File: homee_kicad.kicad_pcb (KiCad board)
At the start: 2 copper layers, 28 parts, among them J1 Screw_Terminal_01x02, J2 USB_B_Micro, J3 Screw_Terminal_01x02, K1 SANYOU_SRD_Form_C, Q2 Q_NPN_Darlington_CBE, T1 Transformer_1P_1S, U1 ESP-01v090, U2 LD1117S33TR_SOT223, U4 PC817

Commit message: j'ai tt fini je suis le goat (PS pas verif par le prof)
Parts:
- removed C4: C, Capacitor_SMD:C_1812_4532Metric
- removed D3, D4, D5, D6, D9: D, Diode_SMD:D_2512_6332Metric
- removed K1: SANYOU_SRD_Form_C, Relay_THT:Relay_SPDT_SANYOU_SRD_Series_Form_C
- removed Q2: Q_NPN_Darlington_CBE, Package_TO_SOT_THT:TO-92
- removed T1: Transformer_1P_1S, WE-PPTI_1006:WE-PPTI_1006_L10.2W6.73H4.19
- added BC1: ~, Connect:Buck Connect, F.Cu at (211.0, 74.5)
- added K2: SANYOU_SRD_Form_A, Relay_THT:Relay_SPST_SANYOU_SRD_Series_Form_A, F.Cu at (184.5, 92.2)
- added Q1: 2N7002, Package_TO_SOT_SMD:SOT-23, F.Cu at (205.5, 84.8)
- C1: value C -> 1uf; footprint Capacitor_SMD:C_1812_4532Metric -> Capacitor_SMD:C_1210_3225Metric
- C2: value C -> 100nf; footprint Capacitor_THT:C_Radial_D6.3mm_H11.0mm_P2.50mm -> Capacitor_SMD:C_1210_3225Metric
- C3: value C -> 100nf; footprint Capacitor_SMD:C_1812_4532Metric -> Capacitor_SMD:C_1210_3225Metric
- D7: footprint Diode_SMD:D_2512_6332Metric -> Diode_SMD:D_1210_3225Metric
- R1: value R -> 150; footprint Resistor_SMD:R_2512_6332Metric -> Resistor_SMD:R_1210_3225Metric
- R4, R5, R6: footprint Resistor_SMD:R_2512_6332Metric -> Resistor_SMD:R_1210_3225Metric
- R7: value R -> 170; footprint Resistor_SMD:R_2512_6332Metric -> Resistor_SMD:R_1210_3225Metric
- R8: value R -> 10k; footprint Resistor_SMD:R_2512_6332Metric -> Resistor_SMD:R_1210_3225Metric
- R9: value R -> 1K; footprint Resistor_SMD:R_2512_6332Metric -> Resistor_SMD:R_1210_3225Metric
- moved R4 144.7 mm to (220.6, 73.8), turned to 180 degrees
- moved R5 144.0 mm to (220.6, 66.7), turned to 180 degrees
- moved R6 143.9 mm to (220.5, 70.3), turned to 180 degrees
- moved R8 124.6 mm to (201.0, 84.8), turned to 90 degrees
- moved R9 119.0 mm to (195.6, 83.3), turned to 180 degrees
- moved J2 117.3 mm to (214.5, 53.8), turned to 180 degrees
- moved C3 115.2 mm to (220.6, 63.0), turned to 180 degrees
- moved R1 110.8 mm to (187.1, 63.2), turned to 180 degrees
- moved C2 104.0 mm to (195.7, 75.8)
- moved R7 98.0 mm to (220.6, 87.0), turned to 0 degrees
- moved C1 93.7 mm to (195.7, 79.2)
- moved U4 92.5 mm to (219.0, 80.0), turned to 180 degrees
- moved U1 90.8 mm to (203.6, 67.8), turned to -90 degrees
- moved D8 79.5 mm to (180.0, 69.2)
- moved D1 79.4 mm to (180.0, 63.2)
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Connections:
- net Net-(U1-UTXD) renamed /TX
- C1 pad 1: Net-(D3-K) -> /GND
- C1 pad 2: GND -> /5V
- C2 pad 1: /VCC -> /GND
- C2 pad 2: GND -> /VCC
- C3 pad 2: GND -> /GND
- D1 pad 1: GND -> /GND
- J2 pad 1: Net-(D9-A) -> /VCC
- J2 pad 5: GND -> /GND
- R8 pad 2: /N IN -> /RELAY
- U1 pad 2: GND -> /GND
- U2 pad 1: GND -> unconnected-(U2-GND-Pad1)
- U2 pad 3: Net-(D3-K) -> /5V
- U4 pad 3: Net-(Q2-B) -> /RELAY
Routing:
- net /GND: track 0.00 -> 68.0 mm, vias 0 -> 2
- net /VCC: track 0.00 -> 67.6 mm, vias 0 -> 2
- net /N IN: track 0.00 -> 62.7 mm, vias 0 -> 1
- net Net-(D7-A): track 0.00 -> 43.5 mm
- net /GPIO0: track 0.00 -> 42.2 mm, vias 0 -> 2
- net /L IN: track 0.00 -> 33.1 mm
- net /RST: track 0.00 -> 30.2 mm
- net /5V: track 0.00 -> 28.3 mm, vias 0 -> 1
- net Net-(J3-Pin_2): track 0.00 -> 25.2 mm
- net Net-(D8-A): track 0.00 -> 23.5 mm
- net /RX: track 0.00 -> 23.3 mm
- net /TX: track 0.00 -> 21.6 mm, vias 0 -> 1
- net /CH_PD: track 0.00 -> 21.0 mm
- net Net-(D7-K): track 0.00 -> 20.7 mm
- net /RELAY: track 0.00 -> 16.5 mm
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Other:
- board outline added: 52.2 x 49.5 mm

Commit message: inte
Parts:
- removed K2: SANYOU_SRD_Form_A, Relay_THT:Relay_SPST_SANYOU_SRD_Series_Form_A
- added K1: ORWH-SH-105D1F,000, Homme:ORWH-1T, F.Cu at (224.5, 92.4)
- D7: footprint Diode_SMD:D_1210_3225Metric -> Diode_SMD:D_1210_3225Metric_Pad1.42x2.65mm_HandSolder
- J2: value USB_B_Micro -> 476421001; footprint Connector_USB:USB_Micro-B_Molex-105017-0001 -> Homme:MOLEX_476421001
- R1, R7: footprint Resistor_SMD:R_1210_3225Metric -> Homme:ERJUP6
- R4, R5, R6, R8, R9: footprint Resistor_SMD:R_1210_3225Metric -> Homme:RESC6332X70N
- moved R6 99.7 mm to (129.4, 110.7), turned to 0 degrees
- moved R5 99.2 mm to (129.4, 105.7), turned to 0 degrees
- moved R4 95.1 mm to (129.4, 100.8), turned to 0 degrees
- moved U4 91.7 mm to (139.4, 125.3), turned to 0 degrees
- moved J2 91.0 mm to (152.3, 120.1), turned to 0 degrees
- moved R8 78.0 mm to (129.4, 115.6), turned to 0 degrees
- moved R9 76.0 mm to (129.4, 120.6), turned to 0 degrees
- moved C3 68.7 mm to (169.4, 108.9), turned to 0 degrees
- moved R7 59.0 mm to (162.2, 95.5)
- moved D1 56.1 mm to (167.5, 118.0)
- moved D8 55.7 mm to (167.5, 123.5)
- moved BC1 53.9 mm to (223.2, 127.0), turned to 0 degrees
- moved J1 51.0 mm to (229.5, 135.5), turned to 180 degrees
- moved D7 41.8 mm to (207.0, 127.0), turned to 180 degrees
- moved U1 40.3 mm to (241.5, 81.4), turned to 0 degrees
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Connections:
- D7 pad 1: Net-(D7-K) -> /5V
- J2 pad 2: unconnected-(J2-D--Pad2) -> /RX
- J2 pad 3: /RX -> unconnected-(J2-D+-Pad3)
- J3 pad 2: Net-(J3-Pin_2) -> /L_OUT
- Q1 pad 2: /N IN -> Net-(D7-A)
- Q1 pad 3: Net-(D7-A) -> /GND
- R7 pad 1: Net-(R7-Pad1) -> /VCC
- R8 pad 1: /N IN -> /GND
- R9 pad 2: Net-(D7-K) -> /5V
- U2 pad 1: unconnected-(U2-GND-Pad1) -> /GND
- U4 pad 4: Net-(R7-Pad1) -> /VCC
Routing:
- net /GND: track 68.0 -> 0.00 mm, vias 2 -> 0
- net /VCC: track 67.6 -> 0.00 mm, vias 2 -> 0
- net /N IN: track 62.7 -> 0.00 mm, vias 1 -> 0
- net Net-(D7-A): track 43.5 -> 0.00 mm
- net /GPIO0: track 42.2 -> 0.00 mm, vias 2 -> 0
- net /L IN: track 33.1 -> 0.00 mm
- net /RST: track 30.2 -> 0.00 mm
- net /5V: track 28.3 -> 0.00 mm, vias 1 -> 0
- net Net-(J3-Pin_2): track 25.2 -> 0.00 mm
- net Net-(D8-A): track 23.5 -> 0.00 mm
- net /RX: track 23.3 -> 0.00 mm
- net /TX: track 21.6 -> 0.00 mm, vias 1 -> 0
- net /CH_PD: track 21.0 -> 0.00 mm
- net Net-(D7-K): track 20.7 -> 0.00 mm
- net /RELAY: track 16.5 -> 0.00 mm
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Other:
- board size 52.2 x 49.5 mm -> 10.8 x 5.5 mm

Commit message: start rework
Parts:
- moved R4 125.5 mm to (251.5, 129.6), turned to 90 degrees
- moved R8 116.6 mm to (243.5, 139.5), turned to 180 degrees
- moved R6 105.6 mm to (234.5, 101.0), turned to -90 degrees
- moved U4 105.5 mm to (244.8, 129.3), turned to -90 degrees
- moved R5 100.7 mm to (230.0, 101.0), turned to -90 degrees
- moved J2 94.0 mm to (241.4, 90.2), turned to 180 degrees
- moved R7 87.3 mm to (246.0, 119.9), turned to -90 degrees
- moved U2 80.4 mm to (234.8, 123.0)
- moved Q1 79.6 mm to (238.6, 132.0), turned to 180 degrees
- moved R9 77.3 mm to (205.1, 104.5), turned to 180 degrees
- moved C3 70.9 mm to (240.0, 102.5), turned to 90 degrees
- moved C2 60.0 mm to (226.4, 123.5), turned to 180 degrees
- moved D8 49.9 mm to (213.6, 104.5), turned to 180 degrees
- moved R1 49.4 mm to (211.1, 98.5), turned to 180 degrees
- moved C1 45.5 mm to (226.3, 127.5), turned to 180 degrees
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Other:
- board size 10.8 x 5.5 mm -> 114 x 85 mm

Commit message: Test W/O routes
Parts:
- BC1: footprint Connect:Buck Connect -> Homme:Buck Connect
- moved R9 39.7 mm to (209.0, 144.1), turned to -90 degrees
- moved D1 33.8 mm to (208.9, 131.8), turned to 90 degrees
- moved C1 32.2 mm to (249.3, 105.0)
- moved R4 31.8 mm to (219.9, 126.2), turned to 0 degrees
- moved D8 31.3 mm to (209.0, 135.5), turned to -90 degrees
- moved R8 30.1 mm to (214.0, 133.4), turned to -90 degrees
- moved R7 28.0 mm to (218.0, 119.4), turned to 0 degrees
- moved C2 26.6 mm to (249.3, 110.0)
- moved Q1 26.0 mm to (214.0, 140.4), turned to -90 degrees
- moved R1 25.4 mm to (208.9, 123.8), turned to -90 degrees
- moved R6 24.4 mm to (214.6, 115.0), turned to 0 degrees
- moved J2 24.3 mm to (218.1, 96.7)
- moved K1 23.9 mm to (232.2, 129.5)
- moved BC1 23.2 mm to (233.0, 129.6), turned to -90 degrees
- moved C3 22.1 mm to (222.0, 115.3), turned to 0 degrees
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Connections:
- net /5V renamed +5V
- net /VCC renamed VCC
- BC1 pad 4: /GND -> GND
- C1 pad 1: /GND -> GND
- C2 pad 1: /GND -> GND
- C3 pad 2: /GND -> GND
- D1 pad 1: /GND -> GND
- J2 pad 5: /GND -> GND
- Q1 pad 2: Net-(D7-A) -> GND
- Q1 pad 3: /GND -> Net-(D7-A)
- R8 pad 1: /GND -> GND
- U1 pad 2: /GND -> GND
- U2 pad 1: /GND -> GND
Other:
- board size 114 x 85 mm -> 10.8 x 5.5 mm

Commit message: Change IO disposition
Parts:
- moved K1 14.1 mm to (224.1, 141.0)
- moved BC1 12.7 mm to (237.9, 141.3)
- moved J2 0.53 mm to (218.5, 97.0)
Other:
- board size 10.8 x 5.5 mm -> 48 x 67.9 mm
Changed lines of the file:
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@@
 	(footprint "Homme:ORWH-1T"
 		(layer "F.Cu")
-		(at 232.1885 129.4615 -90)
+		(at 224.1 141 -90)
 		(descr "ORWH-1T")
 		(tags "Relay or Contactor")
@@
 	(footprint "Homme:Buck Connect"
 		(layer "F.Cu")
-		(at 233 129.56 -90)
+		(at 237.9 141.26 -90)
 		(property "Reference" "BC1"
 			(at 0 -6 -90)
@@
 	(footprint "Homme:MOLEX_476421001"
 		(layer "F.Cu")
-		(at 218.05 96.735 180)
+		(at 218.5 97.015 180)
 		(property "Reference" "J2"
 			(at -0.565 -5.49 0)
@@
 		)
 	)
+	(gr_rect
+		(start 206.9 93.1)
+		(end 254.9 161)
+		(stroke
+			(width 0.05)
+			(type default)
+		)
+		(fill none)
+		(layer "Edge.Cuts")
+	)
 )

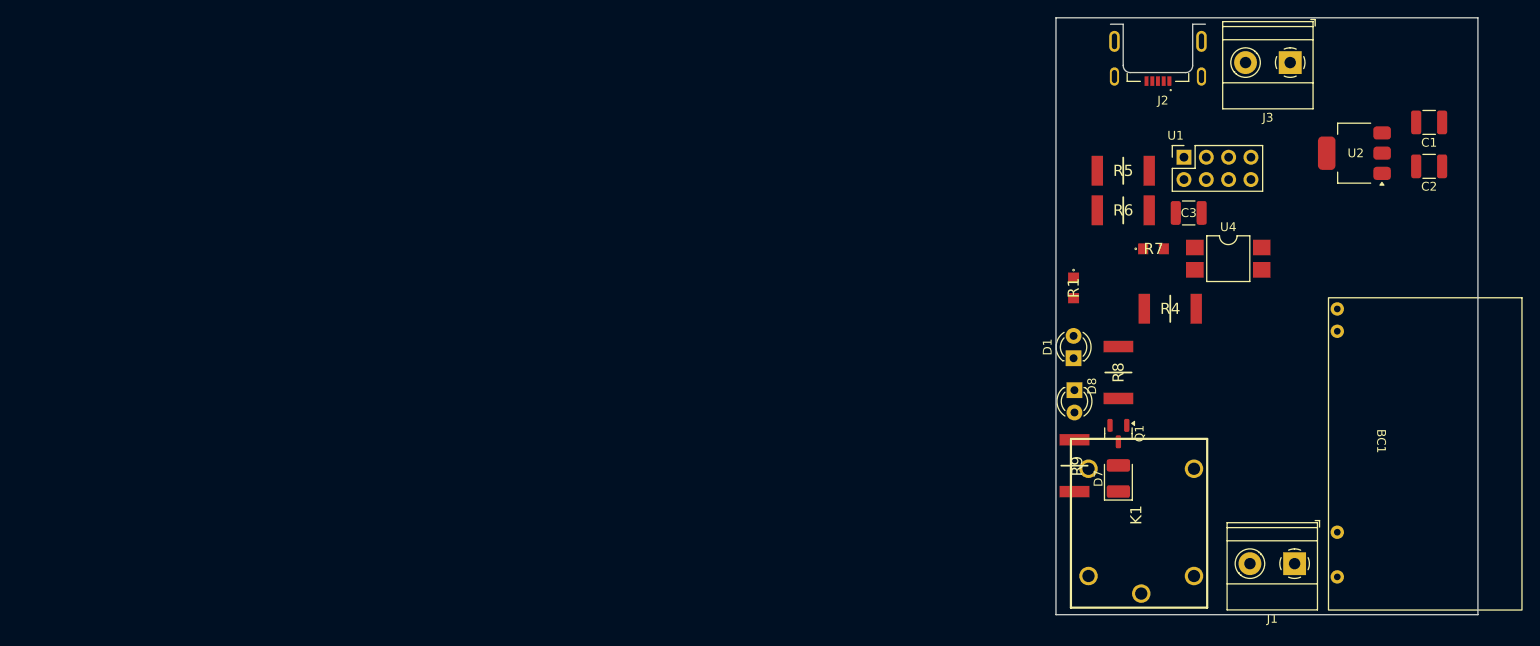
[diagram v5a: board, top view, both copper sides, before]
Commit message: UPDATED TEST W/O ROUTES
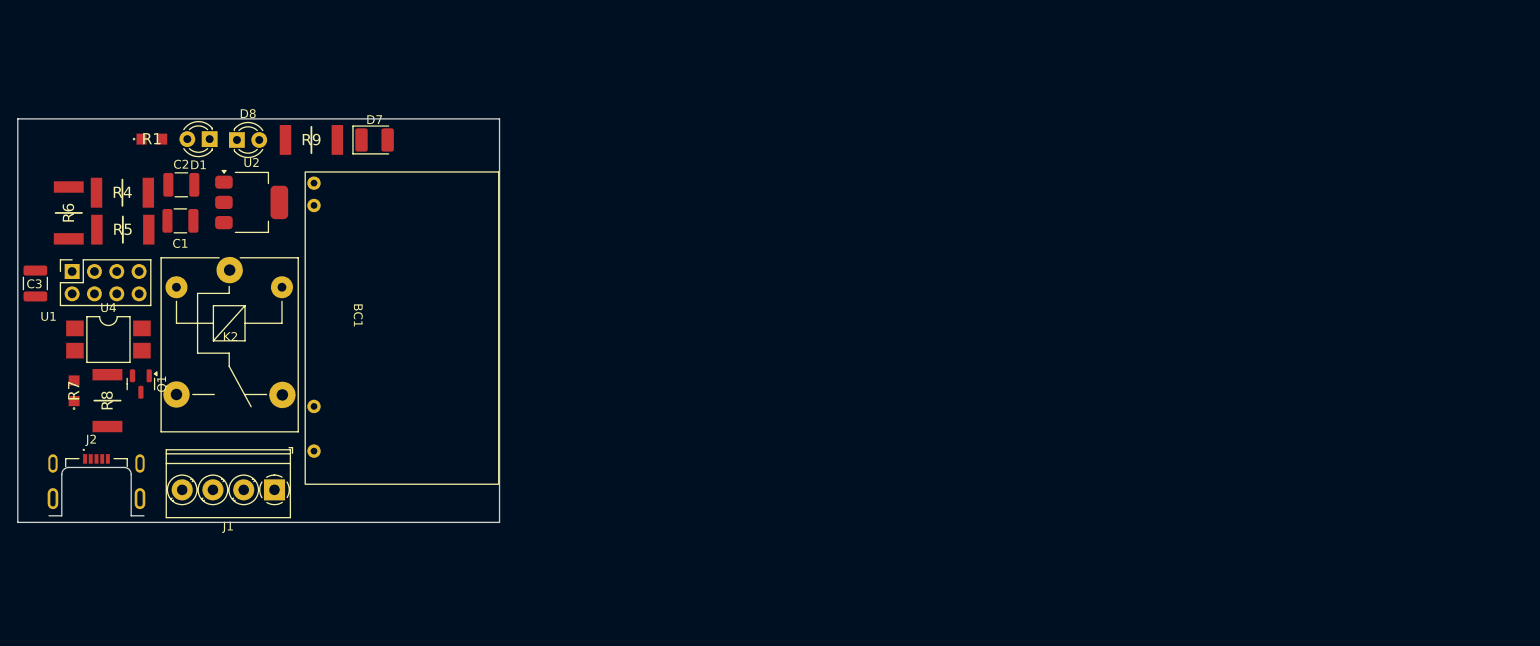
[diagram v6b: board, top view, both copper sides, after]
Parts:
- removed J3: Screw_Terminal_01x02, TerminalBlock_Phoenix:TerminalBlock_Phoenix_MKDS-1,5-2-5.08_1x02_P5.08mm_Horizontal
- removed K1: ORWH-SH-105D1F,000, Homme:ORWH-1T
- added K2: SANYOU_SRD_Form_C, Relay_THT:Relay_SPDT_SANYOU_SRD_Series_Form_C, F.Cu at (112.9, 121.8)
- J1: value Screw_Terminal_01x02 -> Screw_Terminal_01x04; footprint TerminalBlock_Phoenix:TerminalBlock_Phoenix_MKDS-1,5-2-5.08_1x02_P5.08mm_Horizontal -> TerminalBlock_Phoenix:TerminalBlock_Phoenix_PT-1,5-4-3.5-H_1x04_P3.50mm_Horizontal
- moved C1 142.5 mm to (107.3, 116.2), turned to 0 degrees
- moved C2 142.0 mm to (107.4, 112.1), turned to 0 degrees
- moved C3 131.4 mm to (90.8, 123.3), turned to -90 degrees
- moved J2 130.5 mm to (97.8, 146.6), turned to 0 degrees
- moved U4 127.7 mm to (99.1, 129.7)
- moved U1 127.1 mm to (95.0, 122.0)
- moved U2 125.6 mm to (115.4, 114.1), turned to 0 degrees
- moved R7 123.9 mm to (95.2, 135.5), turned to 90 degrees
- moved R6 120.0 mm to (94.6, 115.3), turned to -90 degrees
- moved R4 119.9 mm to (100.7, 113.0), turned to 180 degrees
- moved BC1 117.3 mm to (121.5, 127.0)
- moved J1 116.3 mm to (118.0, 146.8)
- moved R8 115.0 mm to (99.0, 136.7), turned to 90 degrees
- moved R5 114.0 mm to (100.8, 117.2), turned to 180 degrees
- moved Q1 111.3 mm to (102.8, 134.8)
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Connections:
- J1 pad 2: /L IN -> /NC
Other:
- board size 48 x 67.9 mm -> 54.8 x 45.9 mm

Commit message: JOB'S FINISHED ? JOB'S NOT FINISHED
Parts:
- moved J1 10.5 mm to (107.6, 145.5), turned to 0 degrees
- moved R6 8.29 mm to (99.8, 108.8), turned to 180 degrees
- moved R1 1.29 mm to (105.3, 107.2), turned to 90 degrees
- moved R5 1.02 mm to (99.8, 117.4)
- moved R4 0.97 mm to (99.8, 113.2)
- moved C3 0.60 mm to (91.3, 123.0)
- moved D1 0.39 mm to (111.0, 107.0)
- moved Q1 0.12 mm to (102.8, 134.6)
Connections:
- J1 pad 1: /N IN -> /NO
- J1 pad 2: /NC -> /L IN
- J1 pad 3: /L IN -> /NC
- J1 pad 4: /NO -> /N IN
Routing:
- net VCC: track 0.00 -> 69.5 mm
- net GND: track 0.00 -> 59.3 mm, vias 0 -> 2
- net +5V: track 0.00 -> 47.8 mm, vias 0 -> 1
- net /L IN: track 0.00 -> 46.6 mm
- net Net-(D7-A): track 0.00 -> 39.8 mm
- net /TX: track 0.00 -> 26.1 mm
- net /RST: track 0.00 -> 25.0 mm, vias 0 -> 2
- net /GPIO0: track 0.00 -> 22.3 mm
- net /RX: track 0.00 -> 22.0 mm
- net /NC: track 0.00 -> 11.4 mm
- net /NO: track 0.00 -> 9.86 mm
- net /RELAY: track 0.00 -> 8.89 mm
- net Net-(R7-Pad2): track 0.00 -> 7.45 mm
- net /N IN: track 0.00 -> 5.68 mm
- net /CH_PD: track 0.00 -> 4.86 mm
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
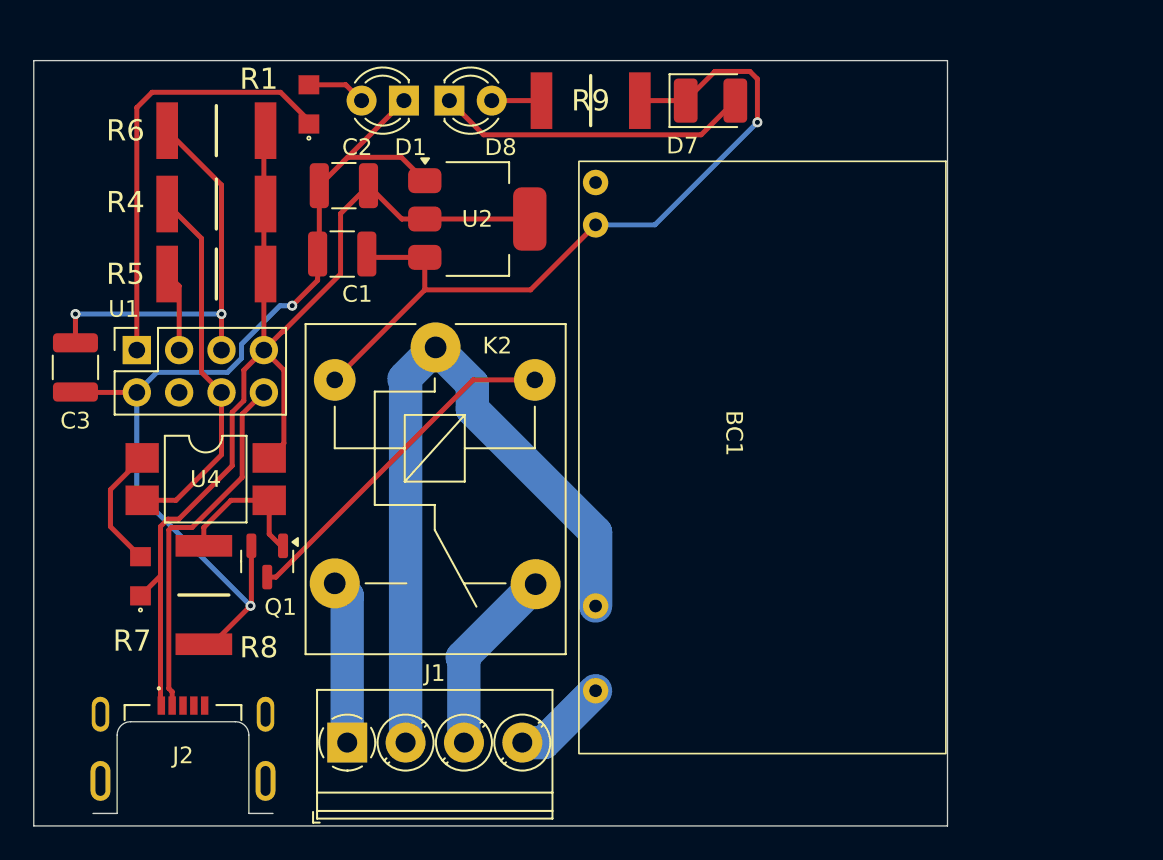
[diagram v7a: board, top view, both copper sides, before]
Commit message: gained 5 min in width
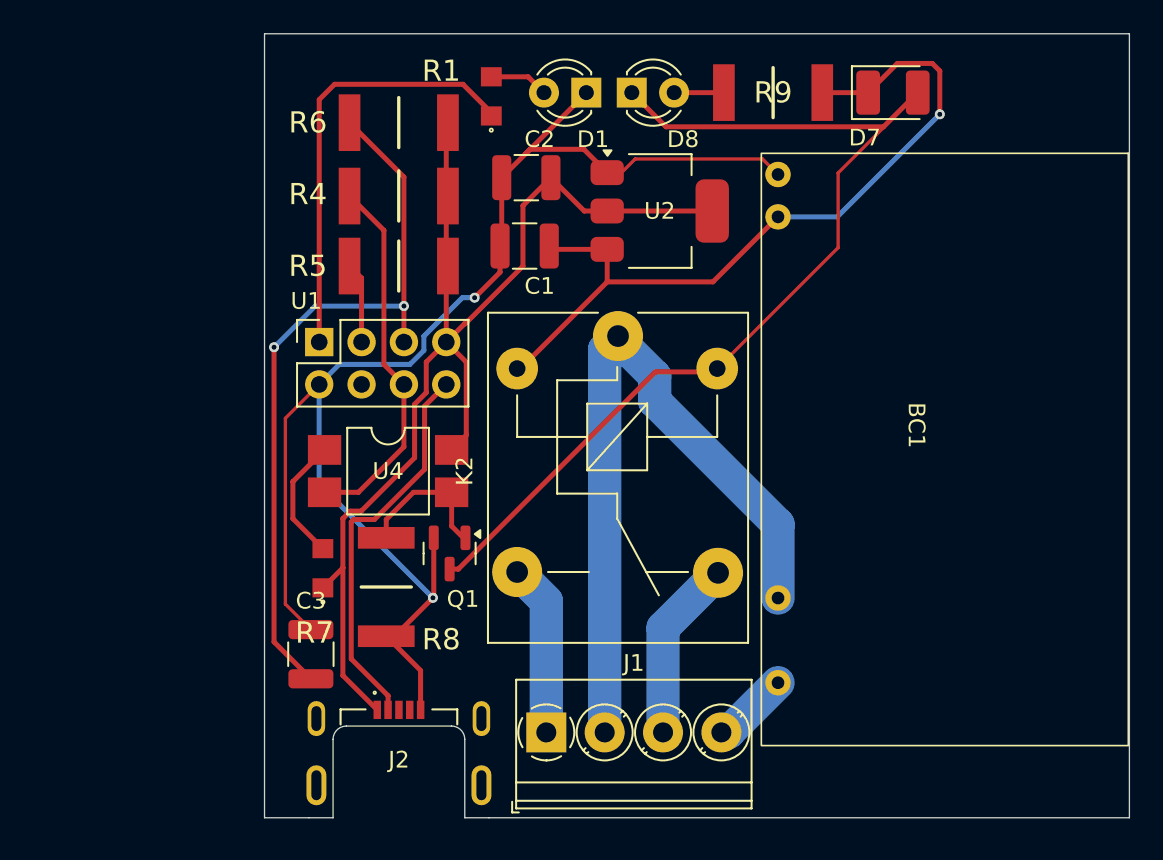
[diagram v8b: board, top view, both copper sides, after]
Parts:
- moved C3 22.3 mm to (105.4, 140.2), turned to 90 degrees
- moved J2 13.0 mm to (110.7, 146.8)
- moved J1 12.0 mm to (119.5, 144.9)
- moved K2 11.0 mm to (123.8, 121.1)
- moved D8 11.0 mm to (124.7, 106.5)
- moved BC1 11.0 mm to (132.4, 126.5)
- moved C1 11.0 mm to (118.2, 115.7)
- moved D1 11.0 mm to (121.9, 106.5)
- moved D7 11.0 mm to (140.3, 106.5)
- moved R4 11.0 mm to (110.7, 112.7)
- moved R5 11.0 mm to (110.7, 116.9)
- moved R6 11.0 mm to (110.7, 108.3)
- moved R7 11.0 mm to (106.1, 135.0)
- moved R8 11.0 mm to (109.9, 136.2)
- moved C2 11.0 mm to (118.3, 111.6)
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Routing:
- net GND: track 59.3 -> 88.1 mm
- net /RST: track 25.0 -> 44.1 mm
- net Net-(D7-A): track 39.8 -> 58.4 mm
- net /L IN: track 46.6 -> 43.6 mm
- net /RX: track 22.0 -> 23.5 mm
- net VCC: track 69.5 -> 71.1 mm
- net /N IN: track 5.68 -> 4.63 mm
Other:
- board size 54.8 x 45.9 mm -> 51.9 x 47 mm
